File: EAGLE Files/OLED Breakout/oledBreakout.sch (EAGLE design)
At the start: 1 part

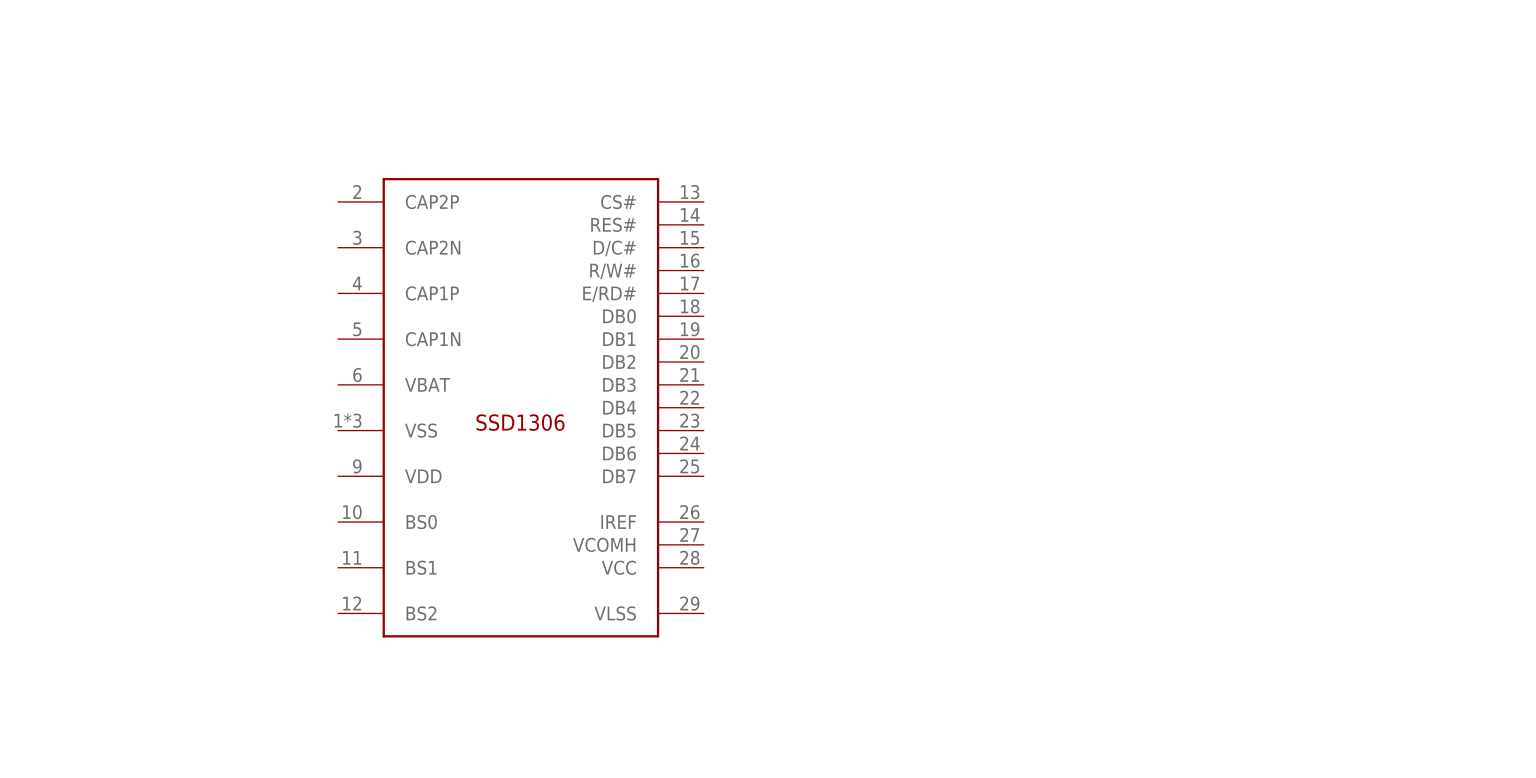
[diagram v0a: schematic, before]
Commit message: OLED breakout mostly finished. Need to merge with power breakout and decide on header/outputs.
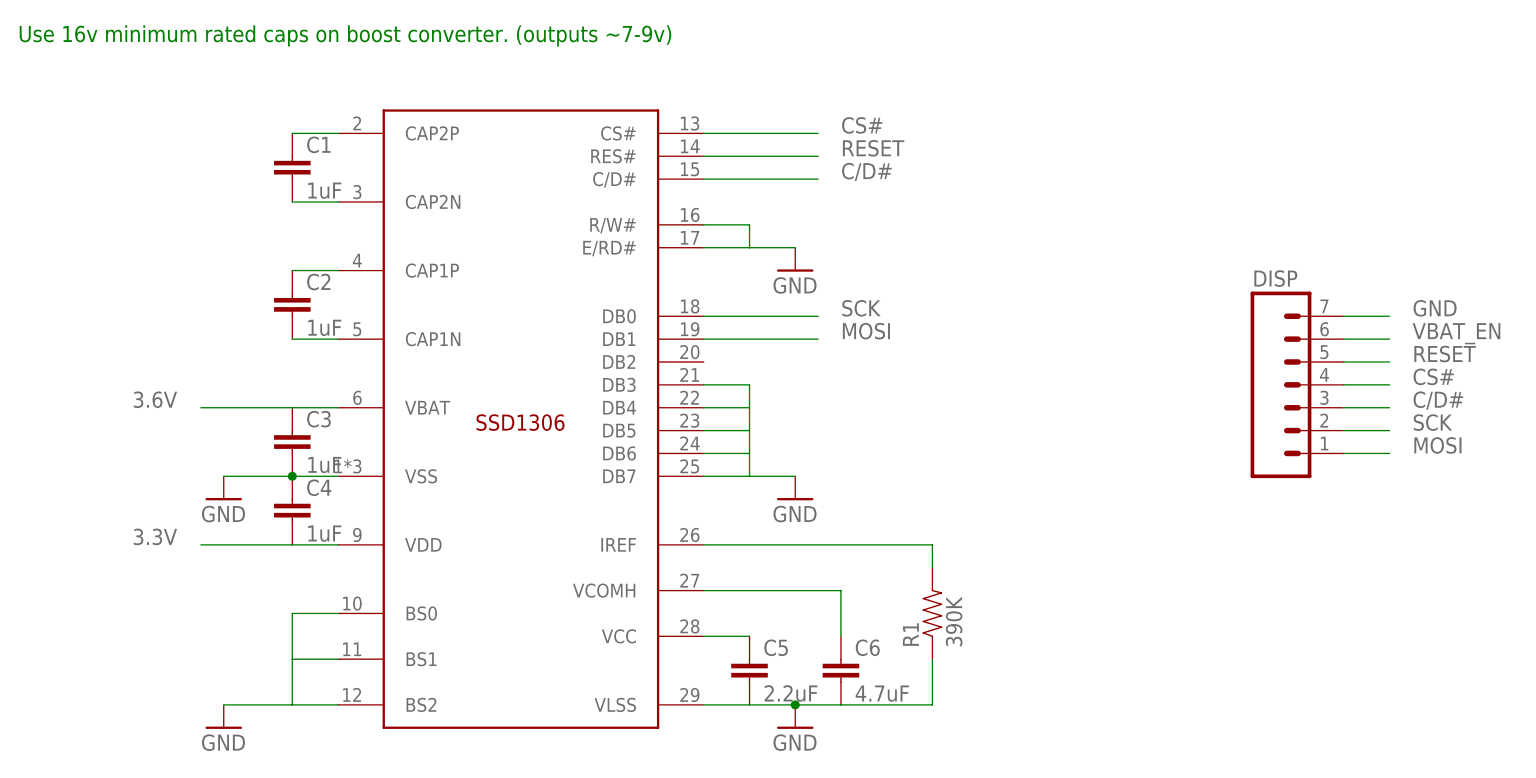
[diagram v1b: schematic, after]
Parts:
- added C1, C2, C3, C4: 1uF, chips:CAP0402-CAP
- added C5: 2.2uF, chips:CAP0402-CAP
- added C6: 4.7uF, chips:CAP0402-CAP
- added DISP: (no value), SparkFun-Connectors:M07LOCK
- added R1: 390K, chips:RESISTOR0402-RES
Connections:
- new net 3.3V: C4.2, U$1.VDD
- new net 3.6V: C3.1, U$1.VBAT
- new net C/D#: DISP.3, U$1.C/D#
- new net CS#: DISP.4, U$1.CS#
- new net GND: C3.2, C4.1, C5.2, C6.2, DISP.7, R1.1, U$1.BS0, U$1.BS1, U$1.BS2, U$1.DB3, U$1.DB4, U$1.DB5, U$1.DB6, U$1.DB7, U$1.E/RD#, U$1.R/W#, U$1.VLSS, U$1.VSS
- new net MOSI: DISP.1, U$1.DB1
- new net N$10: C2.1, U$1.CAP1P
- new net N$11: C1.2, U$1.CAP2N
- new net N$12: C1.1, U$1.CAP2P
- new net N$2: C5.1, U$1.VCC
- new net N$3: C6.1, U$1.VCOMH
- new net N$4: R1.2, U$1.IREF
- new net N$9: C2.2, U$1.CAP1N
- new net RESET: DISP.5, U$1.RES#
- new net SCK: DISP.2, U$1.DB0
- new net VBAT_EN: DISP.6
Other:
- note added: "Use 16v minimum rated caps on boost converter. (outputs ~7-9v)"

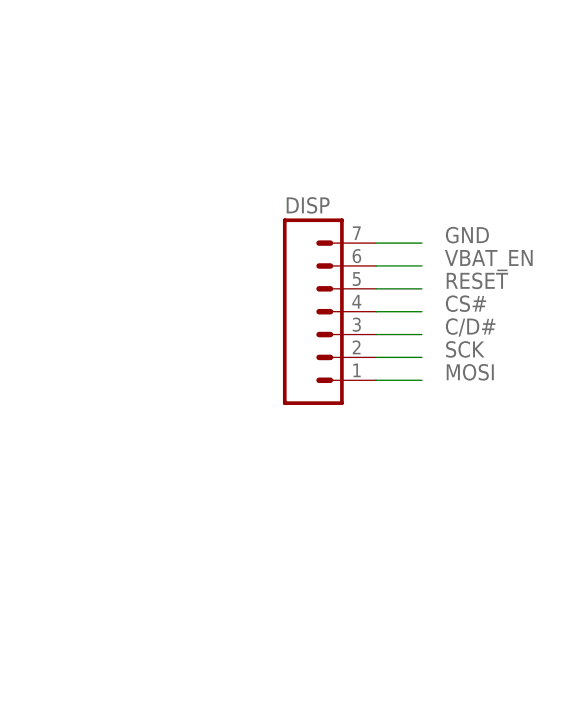
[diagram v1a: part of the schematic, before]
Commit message: Combined power/OLED breakouts. Not yet routed completely.
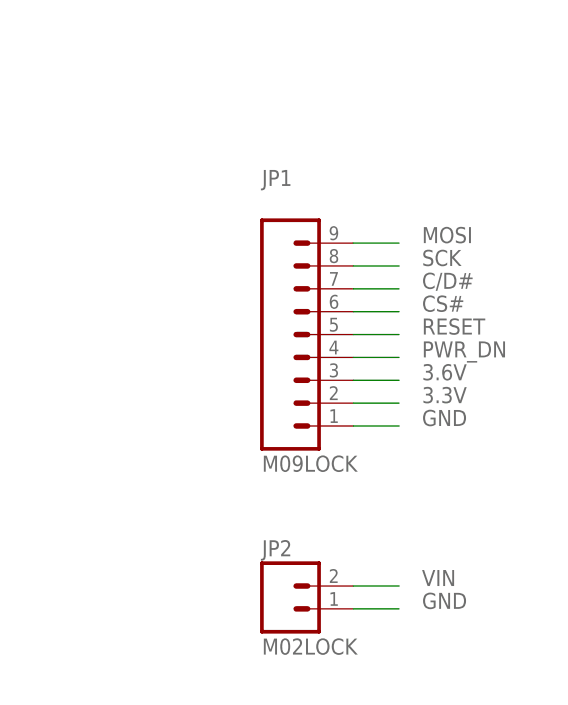
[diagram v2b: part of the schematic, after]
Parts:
- removed DISP: (no value), SparkFun-Connectors:M07LOCK
- added JP1: M09LOCK, SparkFun-Connectors:M09LOCK
- added JP2: M02LOCK, SparkFun-Connectors:M02LOCK
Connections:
- removed net VBAT_EN: DISP.6
- new net PWR_DN: JP1.4
- new net VIN: JP2.2
- net 3.3V: now also JP1.2
- net 3.6V: now also JP1.3
- net C/D#: now also JP1.7; no longer DISP.3
- net CS#: now also JP1.6; no longer DISP.4
- net GND: now also JP1.1, JP2.1; no longer DISP.7
- net MOSI: now also JP1.9; no longer DISP.1
- net RESET: now also JP1.5; no longer DISP.5
- net SCK: now also JP1.8; no longer DISP.2
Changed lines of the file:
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@@
 <part name="GND4" library="supply1" deviceset="GND" device=""/>
 <part name="GND5" library="supply1" deviceset="GND" device=""/>
-<part name="DISP" library="SparkFun-Connectors" deviceset="M07" device="LOCK"/>
+<part name="JP1" library="SparkFun-Connectors" deviceset="M09" device="LOCK"/>
+<part name="JP2" library="SparkFun-Connectors" deviceset="M02" device="LOCK"/>
 </parts>
 <sheets>
@@
 <instance part="GND4" gate="1" x="43.18" y="35.56"/>
 <instance part="GND5" gate="1" x="43.18" y="10.16"/>
-<instance part="DISP" gate="G$1" x="162.56" y="45.72"/>
+<instance part="JP1" gate="G$1" x="154.94" y="45.72"/>
+<instance part="JP2" gate="G$1" x="157.48" y="15.24"/>
 </instances>
 <busses>
@@
 </segment>
 <segment>
-<pinref part="DISP" gate="G$1" pin="7"/>
-<wire x1="167.64" y1="55.88" x2="172.72" y2="55.88" width="0.1524" layer="91"/>
-<label x="175.26" y="55.88" size="1.778" layer="95"/>
+<pinref part="JP1" gate="G$1" pin="1"/>
+<wire x1="165.1" y1="35.56" x2="170.18" y2="35.56" width="0.1524" layer="91"/>
+<label x="172.72" y="35.56" size="1.778" layer="95"/>
+</segment>
+<segment>
+<pinref part="JP2" gate="G$1" pin="1"/>
+<wire x1="165.1" y1="15.24" x2="170.18" y2="15.24" width="0.1524" layer="91"/>
+<label x="172.72" y="15.24" size="1.778" layer="95"/>
 </segment>
 </net>
@@
 <label x="33.02" y="45.72" size="1.778" layer="95"/>
 </segment>
+<segment>
+<pinref part="JP1" gate="G$1" pin="3"/>
+<wire x1="165.1" y1="40.64" x2="170.18" y2="40.64" width="0.1524" layer="91"/>
+<label x="172.72" y="40.64" size="1.778" layer="95"/>
+</segment>
 </net>
 <net name="3.3V" class="0">
@@
 <label x="33.02" y="30.48" size="1.778" layer="95"/>
 </segment>
+<segment>
+<pinref part="JP1" gate="G$1" pin="2"/>
+<wire x1="165.1" y1="38.1" x2="170.18" y2="38.1" width="0.1524" layer="91"/>
+<label x="172.72" y="38.1" size="1.778" layer="95"/>
+</segment>
 </net>
 <net name="N$9" class="0">
@@
 </segment>
 <segment>
-<pinref part="DISP" gate="G$1" pin="4"/>
-<wire x1="167.64" y1="48.26" x2="172.72" y2="48.26" width="0.1524" layer="91"/>
-<label x="175.26" y="48.26" size="1.778" layer="95"/>
+<pinref part="JP1" gate="G$1" pin="6"/>
+<wire x1="165.1" y1="48.26" x2="170.18" y2="48.26" width="0.1524" layer="91"/>
+<label x="172.72" y="48.26" size="1.778" layer="95"/>
 </segment>
 </net>
@@
 </segment>
 <segment>
-<pinref part="DISP" gate="G$1" pin="5"/>
-<wire x1="167.64" y1="50.8" x2="172.72" y2="50.8" width="0.1524" layer="91"/>
-<label x="175.26" y="50.8" size="1.778" layer="95"/>
+<pinref part="JP1" gate="G$1" pin="5"/>
+<wire x1="165.1" y1="45.72" x2="170.18" y2="45.72" width="0.1524" layer="91"/>
+<label x="172.72" y="45.72" size="1.778" layer="95"/>
 </segment>
 </net>
@@
 </segment>
 <segment>
-<pinref part="DISP" gate="G$1" pin="3"/>
-<wire x1="167.64" y1="45.72" x2="172.72" y2="45.72" width="0.1524" layer="91"/>
-<label x="175.26" y="45.72" size="1.778" layer="95"/>
+<pinref part="JP1" gate="G$1" pin="7"/>
+<wire x1="165.1" y1="50.8" x2="170.18" y2="50.8" width="0.1524" layer="91"/>
+<label x="172.72" y="50.8" size="1.778" layer="95"/>
 </segment>
 </net>
@@
 </segment>
 <segment>
-<pinref part="DISP" gate="G$1" pin="2"/>
-<wire x1="167.64" y1="43.18" x2="172.72" y2="43.18" width="0.1524" layer="91"/>
-<label x="175.26" y="43.18" size="1.778" layer="95"/>
+<pinref part="JP1" gate="G$1" pin="8"/>
+<wire x1="165.1" y1="53.34" x2="170.18" y2="53.34" width="0.1524" layer="91"/>
+<label x="172.72" y="53.34" size="1.778" layer="95"/>
 </segment>
 </net>
@@
 </segment>
 <segment>
-<pinref part="DISP" gate="G$1" pin="1"/>
-<wire x1="167.64" y1="40.64" x2="172.72" y2="40.64" width="0.1524" layer="91"/>
-<label x="175.26" y="40.64" size="1.778" layer="95"/>
-</segment>
-</net>
-<net name="VBAT_EN" class="0">
-<segment>
-<pinref part="DISP" gate="G$1" pin="6"/>
-<wire x1="167.64" y1="53.34" x2="172.72" y2="53.34" width="0.1524" layer="91"/>
-<label x="175.26" y="53.34" size="1.778" layer="95"/>
-</segment>
-</net>
+<pinref part="JP1" gate="G$1" pin="9"/>
+<wire x1="165.1" y1="55.88" x2="170.18" y2="55.88" width="0.1524" layer="91"/>
+<label x="172.72" y="55.88" size="1.778" layer="95"/>
+</segment>
+</net>
+<net name="PWR_DN" class="0">
+<segment>
+<pinref part="JP1" gate="G$1" pin="4"/>
+<wire x1="165.1" y1="43.18" x2="170.18" y2="43.18" width="0.1524" layer="91"/>
+<label x="172.72" y="43.18" size="1.778" layer="95"/>
+</segment>
+</net>
+<net name="VIN" class="0">
+<segment>
+<pinref part="JP2" gate="G$1" pin="2"/>
+<wire x1="165.1" y1="17.78" x2="170.18" y2="17.78" width="0.1524" layer="91"/>
+<label x="172.72" y="17.78" size="1.778" layer="95"/>
+</segment>
+</net>
